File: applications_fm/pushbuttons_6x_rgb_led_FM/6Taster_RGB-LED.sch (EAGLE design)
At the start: 19 parts, among them U1 WS2803

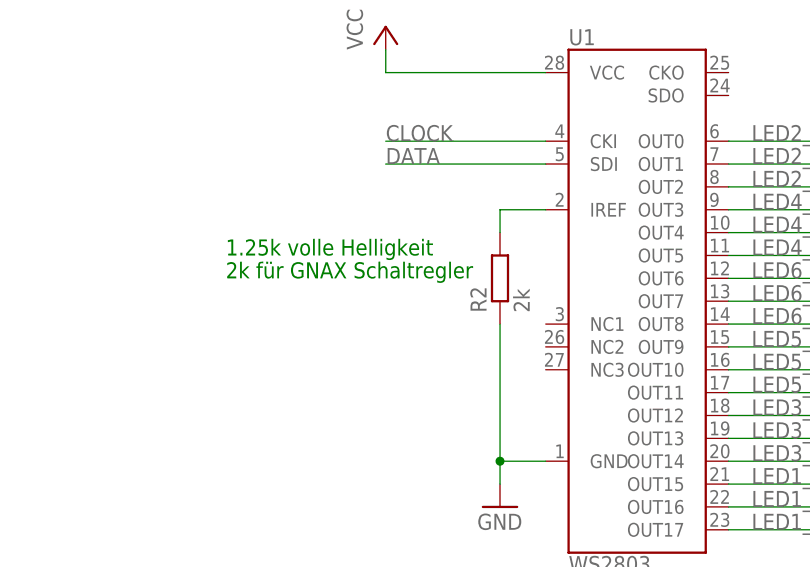
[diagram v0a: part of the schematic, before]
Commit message: Correction of resitor value
The brighntess of the LEDs is controlled by a resistor. The value is corrected now.
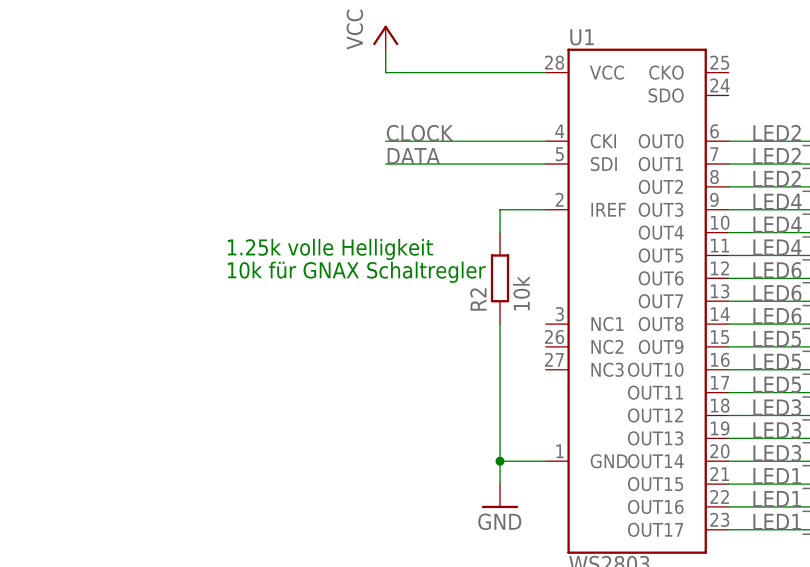
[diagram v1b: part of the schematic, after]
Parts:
- R2: value 2k -> 10k
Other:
- note added: "10k für GNAX Schaltregler"
- note removed: "2k für GNAX Schaltregler"
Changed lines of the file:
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@@
 <part name="D2" library="IR_LED_Photodiode_KNX_Taster" deviceset="BPW34FAS" device=""/>
 <part name="D1" library="IR_LED_Photodiode_KNX_Taster" deviceset="SFH4640" device=""/>
-<part name="R2" library="rcl" deviceset="R-EU_" device="R0805" value="2k"/>
+<part name="R2" library="rcl" deviceset="R-EU_" device="R0805" value="10k"/>
 <part name="C1" library="rcl" deviceset="C-EU" device="C0805" value="1n"/>
 <part name="GND10" library="supply1" deviceset="GND" device=""/>
@@
 <text x="292.1" y="180.34" size="1.778" layer="91">Vorwiderstand von 100 ist auf GNAX Board enthalten</text>
 <text x="154.94" y="83.82" size="1.778" layer="91">1.25k volle Helligkeit</text>
-<text x="154.94" y="81.28" size="1.778" layer="91">2k für GNAX Schaltregler</text>
+<text x="154.94" y="81.28" size="1.778" layer="91">10k für GNAX Schaltregler</text>
 </plain>
 <instances>
